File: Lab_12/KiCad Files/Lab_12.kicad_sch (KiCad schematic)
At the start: 35 parts

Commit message: Continue Lab 12
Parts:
- added C? (x2): 0.01uF, symbol Device:C
- added D?: 9.1V, symbol Device:D_Zener
- added LD?: D_Laser_1C2A, symbol Device:D_Laser_1C2A
- added Q?: Q_NPN_EBC, symbol Device:Q_NPN_EBC
- added R?: 100K, Resistor_THT:R_Axial_DIN0207_L6.3mm_D2.5mm_P7.62mm_Horizontal, symbol Device:R
- added R? (x2): 1K, Resistor_THT:R_Axial_DIN0207_L6.3mm_D2.5mm_P7.62mm_Horizontal, symbol Device:R
- added R?: 330K, Resistor_THT:R_Axial_DIN0207_L6.3mm_D2.5mm_P7.62mm_Horizontal, symbol Device:R
- added R?: 10K, Resistor_THT:R_Axial_DIN0207_L6.3mm_D2.5mm_P7.62mm_Horizontal, symbol Device:R
- added SC?: Solar_Cell, symbol Device:Solar_Cell
- added U? (x3): TLV272, symbol Amplifier_Operational:TLV2372
- D?: value 5.1V -> 6.2V
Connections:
- net GND: now also C?.2, Q?.1 (E), R?.2, R?.2, SC?.2 (-), U?.4 (V-)
- net V_Supply: now also D?.1 (K)
- net at U?.1: now also C?.1, R?.1
- net at U?.2: now also R?.1, R?.2
- net +5V renamed +6V
- net +6V: now also U?.8 (V+)
- new net: C?.1, SC?.1 (+)
- new net: Q?.2 (B), R?.2
- new net: LD?.1 (K), Q?.3 (C)
- new net: C?.2, R?.1, U?.3 (+)
- new net: D?.2 (A), LD?.2 (A)
- new net: R?.1, U?.1
- new net: R?.1, R?.2, U?.2 (-)
- no-connect marks 11 -> 13
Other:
- note added: "Laser Driver"
- moved on the sheet: C?, D?, M?, R?, RV?, U?, U?A, U?B, U?C, U?D, U?E, U?F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

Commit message: Continue Lab 12 Schema
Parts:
- removed R?: 680K, Resistor_THT:R_Axial_DIN0207_L6.3mm_D2.5mm_P7.62mm_Horizontal, symbol Device:R
- removed U? (x3): TLV272, symbol Amplifier_Operational:TLV2372
- added C? (x3): 0.22uF, symbol Device:C
- added C?: 0.1uF, symbol Device:C
- added D? (x2): 1N4148, symbol Device:D
- added R?: 680K, Resistor_THT:R_Axial_DIN0207_L6.3mm_D2.5mm_P7.62mm_Horizontal, symbol Device:R
- added R? (x6): 100K, Resistor_THT:R_Axial_DIN0207_L6.3mm_D2.5mm_P7.62mm_Horizontal, symbol Device:R
- added R? (x2): 6K8, Resistor_THT:R_Axial_DIN0207_L6.3mm_D2.5mm_P7.62mm_Horizontal, symbol Device:R
- added R?: 270K, Resistor_THT:R_Axial_DIN0207_L6.3mm_D2.5mm_P7.62mm_Horizontal, symbol Device:R
- added R?: 470K, Resistor_THT:R_Axial_DIN0207_L6.3mm_D2.5mm_P7.62mm_Horizontal, symbol Device:R
- added R? (x2): 4M7, Resistor_THT:R_Axial_DIN0207_L6.3mm_D2.5mm_P7.62mm_Horizontal, symbol Device:R
- added R? (x2): 4K7, Resistor_THT:R_Axial_DIN0207_L6.3mm_D2.5mm_P7.62mm_Horizontal, symbol Device:R
- added R? (x2): 2M2, Resistor_THT:R_Axial_DIN0207_L6.3mm_D2.5mm_P7.62mm_Horizontal, symbol Device:R
- added R?: 47K, Resistor_THT:R_Axial_DIN0207_L6.3mm_D2.5mm_P7.62mm_Horizontal, symbol Device:R
- added R?: 1K, Resistor_THT:R_Axial_DIN0207_L6.3mm_D2.5mm_P7.62mm_Horizontal, symbol Device:R
- added RV? (x2): 200K, symbol Device:R_Potentiometer_Trim
- added RV?: 100K, symbol Device:R_Potentiometer_Trim
- added RV? (x2): 500K, SamacSys_Parts:3386P1503, symbol Device:R_Potentiometer_Trim
- added RV?: 100K, symbol Device:R_Potentiometer
- added RV?: 100K, SamacSys_Parts:3386P1503, symbol Device:R_Potentiometer_Trim
- added SW?: CW, symbol Switch:SW_Push
- added SW?: CCW, symbol Switch:SW_Push
- added U? (x3): TLV272, symbol Amplifier_Operational:TLV2372
- R?: value 1K -> 10K
- R?: value 330K -> 3M3
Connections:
- net +6V: now also RV?.1, U?.9 (EN3,4), R?.1, R?.1, R?.1, RV?.1, SW?.2, U?.8 (V+); no longer U?.1 (EN1,2)
- net GND: now also RV?.3, C?.2, C?.2, R?.2, R?.2, RV?.2, RV?.3, RV?.3, SW?.1, U?.4 (V-)
- net at RV?.2: now also R?.1
- net at U?.10 (3A): now also U?.8
- net at U?.11 (3Y): now also C?.1, M?.1 (+)
- net at U?.14 (4Y): now also C?.2, M?.2 (-)
- net at U?.15 (4A): now also R?.2, R?.2, U?.1, U?.9
- net at U?.2 (1A): no longer U?.8
- net at C?.2, R?.1: now also U?.3 (+)
- net at R?.1, U?.14 (X): now also R?.1, R?.2
- net at R?.1: now also U?.10 (-), C?.1, D?.1 (K), R?.1, R?.1
- net at R?.1, R?.2: now also U?.2 (-)
- net at U?.11 (+): now also R?.1, RV?.2
- net at U?.13: now also U?.11 (A), D?.1 (K), R?.2, R?.2
- net at U?.12 (X0): now also U?.14, R?.2
- net at U?.13 (X1): now also U?.12
- net at U?.13: now also RV?.2
- net SGND: now reaches U?.5 (+)
- net SGND: now also U?.10 (+), U?.12 (+), U?.3 (+), C?.1, R?.1, R?.1, R?.2
- net at U?.6 (-): now also C?.1, RV?.1, RV?.2
- net at U?.7: now also C?.2, R?.1
- net at U?.13 (-): now also R?.1, R?.2, R?.2, R?.2
- new net: R?.2, RV?.1
- new net: R?.1, RV?.1, RV?.2, U?.1
- new net: R?.2, R?.2, U?.5 (+)
- new net: C?.1, R?.2
- new net: C?.2, RV?.3, U?.9 (-)
- new net: RV?.1, RV?.3
- new net: R?.2, SW?.2
- new net: D?.2 (A), U?.1
- new net: R?.1, RV?.1, RV?.2, U?.8
- new net: RV?.1, RV?.2, RV?.3
- new net: R?.1, R?.2, U?.6 (-)
- new net: R?.1, R?.1, R?.2, RV?.3, U?.7
- new net: R?.1, SW?.1
- new net: R?.2, RV?.3, U?.2 (-)
- now unconnected: U?.3 (1Y), U?.6 (2Y), U?.7 (2A)
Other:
- note added: "D"
- note added: "Error Amplifier"
- note added: "Feedback Mux & Jog Control"
- note added: "High Rotation Limit Trim"
- note added: "I"
- note added: "Laser Presence Detector"
- note added: "Laser Presence Threshold Trim"
- note added: "Low Rotation Limit Trim"
- note added: "P"
- note added: "P.I.D. Controller"
- note added: "Peak Detector"
- note added: "Setpoint Trim"
- note added: "Solar Cell Filter & Amplifier"
- note added: "~1kHz Pulse"
- note removed: "Voltage Feedback"
- moved on the sheet: C?, D?, LD?, M?, Q?, R?, RV?, SC?, U?, U?A, U?B, U?C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

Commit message: Finish Lab 12 Schema Rev1
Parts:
- removed D?: 1N4148, symbol Device:D
- removed R?: 6K8, Resistor_THT:R_Axial_DIN0207_L6.3mm_D2.5mm_P7.62mm_Horizontal, symbol Device:R
- removed RV? (x2): 200K, symbol Device:R_Potentiometer_Trim
- added R15, R16: 1M5, Resistor_THT:R_Axial_DIN0207_L6.3mm_D2.5mm_P7.62mm_Horizontal, symbol Device:R
- C1, C2, C4: renamed from C?; footprint (none) -> Capacitor_THT:C_Rect_L16.5mm_W4.7mm_P15.00mm_MKT
- C3, C5, C6, C8, C9: renamed from C?; footprint (none) -> Capacitor_THT:C_Disc_D9.0mm_W2.5mm_P5.00mm
- C7: renamed from C?; footprint (none) -> Capacitor_THT:C_Disc_D9.0mm_W5.0mm_P10.00mm
- D1, D2: renamed from D?; footprint (none) -> Diode_THT:D_A-405_P7.62mm_Horizontal
- D3: renamed from D?; footprint (none) -> Diode_THT:D_A-405_P12.70mm_Horizontal
- LD1: renamed from LD?; footprint (none) -> Connector_PinHeader_2.54mm:PinHeader_1x02_P2.54mm_Vertical
- M1: renamed from M?; footprint (none) -> Connector_PinHeader_2.54mm:PinHeader_1x02_P2.54mm_Vertical
- Q1: renamed from Q?; value Q_NPN_EBC -> 2N4401; footprint (none) -> Package_TO_SOT_THT:TO-92L_Inline_Wide
- R29: renamed from R?; footprint Resistor_THT:R_Axial_DIN0207_L6.3mm_D2.5mm_P7.62mm_Horizontal -> Resistor_THT:R_Axial_DIN0207_L6.3mm_D2.5mm_P2.54mm_Vertical
- R3: renamed from R?; footprint Resistor_THT:R_Axial_DIN0207_L6.3mm_D2.5mm_P7.62mm_Horizontal -> Resistor_THT:R_Axial_DIN0207_L6.3mm_D2.5mm_P10.16mm_Horizontal
- RV1: renamed from RV?; value 100K -> 2M; footprint (none) -> Connector_PinHeader_2.54mm:PinHeader_1x03_P2.54mm_Vertical
- RV6: renamed from RV?; footprint (none) -> SamacSys_Parts:3386P1503
- SC1: renamed from SC?; footprint (none) -> Connector_PinHeader_2.54mm:PinHeader_1x02_P2.54mm_Vertical
- SW1, SW2: renamed from SW?; footprint (none) -> Button_Switch_THT:SW_PUSH_6mm_H9.5mm
- U1: renamed from U?; footprint (none) -> Package_DIP:DIP-8_W7.62mm
- U2, U3, U4: renamed from U?; footprint (none) -> Package_DIP:DIP-14_W7.62mm
- U5: renamed from U?; footprint (none) -> Package_DIP:DIP-16_W7.62mm
- gave numbers to parts that had none: 35
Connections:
- net +6V: now also R15.1
- net GND: now also R16.2
- net at RV1.3: now also R16.1
- net at RV1.1: now also R15.2
- no-connect marks 13 -> 22
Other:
- note added: "Scanning Circuitry"
- note removed: "High Rotation Limit Trim"
- note removed: "Low Rotation Limit Trim"
- moved on the sheet: RV1, U3B, U3C, U3E, U3F, U4D

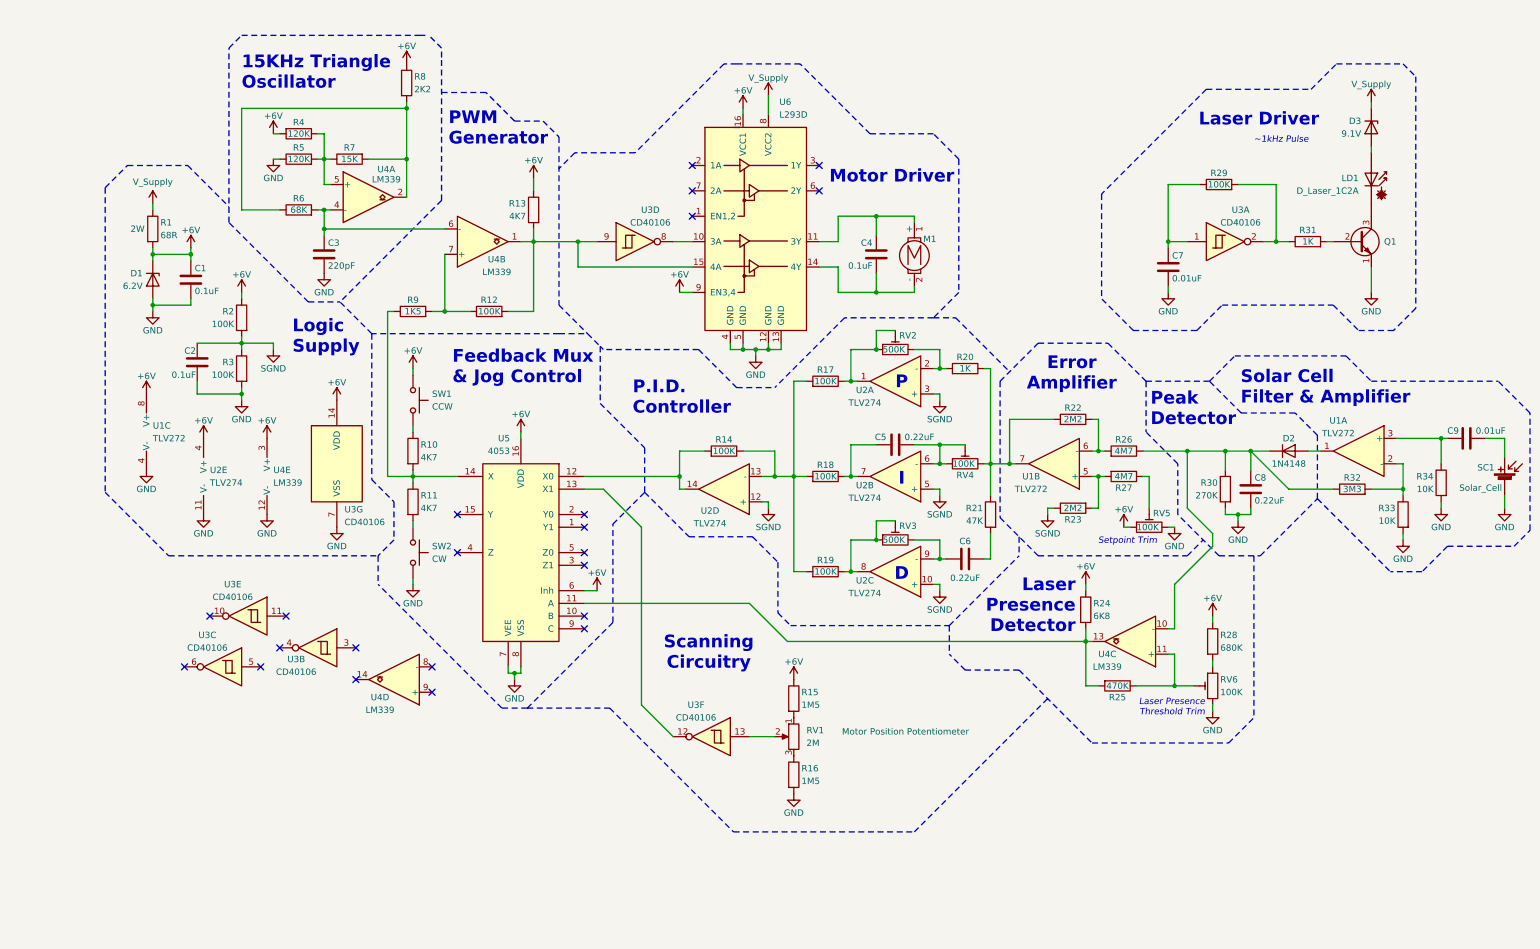
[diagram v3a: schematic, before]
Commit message: Connect Unused 40106 Inputs to GND
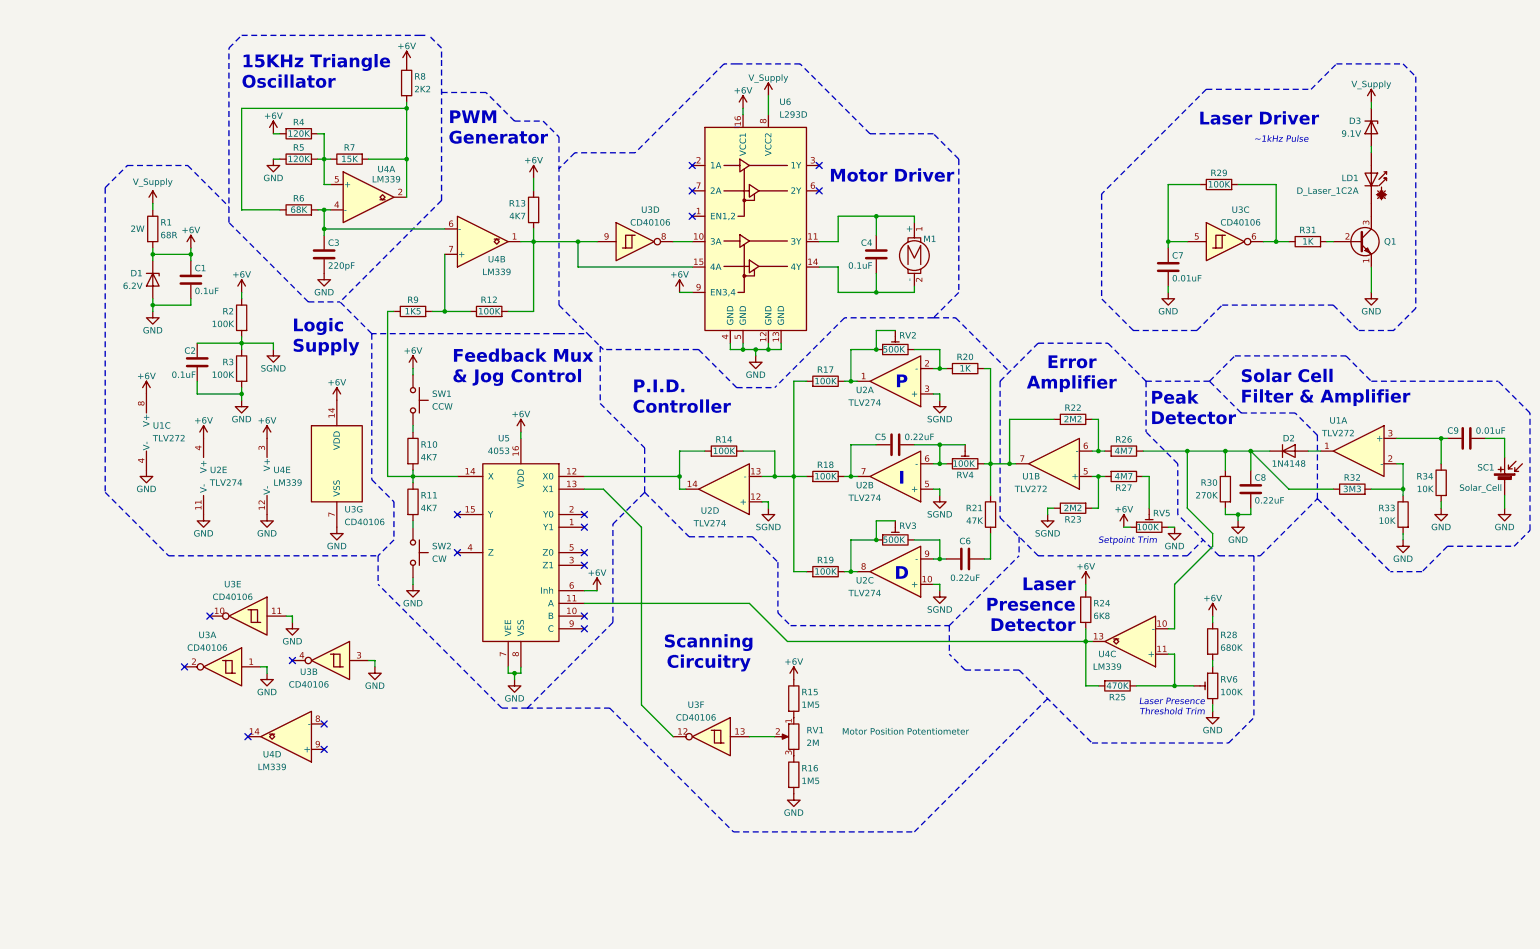
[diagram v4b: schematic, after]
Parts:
- C8: footprint Capacitor_THT:C_Disc_D9.0mm_W2.5mm_P5.00mm -> Capacitor_THT:C_Disc_D9.0mm_W5.0mm_P7.50mm
- D2: footprint Diode_THT:D_A-405_P7.62mm_Horizontal -> Diode_THT:D_A-405_P2.54mm_Vertical_AnodeUp
- R12, R25, R31, R32, R6: footprint Resistor_THT:R_Axial_DIN0207_L6.3mm_D2.5mm_P7.62mm_Horizontal -> Resistor_THT:R_Axial_DIN0207_L6.3mm_D2.5mm_P5.08mm_Vertical
- R13, R24, R28, R33, R34, R5: footprint Resistor_THT:R_Axial_DIN0207_L6.3mm_D2.5mm_P7.62mm_Horizontal -> Resistor_THT:R_Axial_DIN0207_L6.3mm_D2.5mm_P10.16mm_Horizontal
- R14, R17, R18, R21, R22: footprint Resistor_THT:R_Axial_DIN0207_L6.3mm_D2.5mm_P7.62mm_Horizontal -> Resistor_THT:R_Axial_DIN0207_L6.3mm_D2.5mm_P2.54mm_Vertical
- R19, R23: footprint Resistor_THT:R_Axial_DIN0207_L6.3mm_D2.5mm_P7.62mm_Horizontal -> Resistor_THT:R_Axial_DIN0207_L6.3mm_D2.5mm_P15.24mm_Horizontal
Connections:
- net GND: now also U3.1, U3.11, U3.3
- net at C7.1, R29.1: now also U3.5; no longer U3.1
- net at R29.2, R31.1: now also U3.6; no longer U3.2
- no-connect marks 22 -> 19
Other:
- moved on the sheet: U3B, U4D

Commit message: Finish Lab 12
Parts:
- removed R15: 1M5, Resistor_THT:R_Axial_DIN0207_L6.3mm_D2.5mm_P7.62mm_Horizontal, symbol Device:R
- added R14: 2K2, Resistor_THT:R_Axial_DIN0207_L6.3mm_D2.5mm_P10.16mm_Horizontal, symbol Device:R
- added R20, R21: 120K, Resistor_THT:R_Axial_DIN0207_L6.3mm_D2.5mm_P10.16mm_Horizontal, symbol Device:R
- C3: value 220pF -> 100pF
- R16: value 1M5 -> 15K; footprint Resistor_THT:R_Axial_DIN0207_L6.3mm_D2.5mm_P7.62mm_Horizontal -> Resistor_THT:R_Axial_DIN0207_L6.3mm_D2.5mm_P5.08mm_Vertical
- R27: renamed from R25; footprint Resistor_THT:R_Axial_DIN0207_L6.3mm_D2.5mm_P5.08mm_Vertical -> Resistor_THT:R_Axial_DIN0207_L6.3mm_D2.5mm_P15.24mm_Horizontal
- renumbered R14 to R15, R20 to R22, R21 to R23, R22 to R24, R23 to R25, R24 to R26, R26 to R28, R27 to R29, R28 to R30, R29 to R31, R30 to R32, R31 to R33, R32 to R34, R33 to R35, R34 to R36
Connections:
- net +6V: now also RV1.1, R14.1, R20.1
- net GND: now also RV1.3, RV6.1, U3.13, R21.2; no longer R16.2, RV6.3
- net at R30.2: now also RV6.3; no longer RV6.1
- net at R26.2, R27.2, U5.11 (A): now also U4.14; no longer U4.13
- net at C8.1, D2.1 (K), R28.1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: now also U4.8 (-); no longer U4.10 (-)
- net at R27.1, RV6.2: now also U4.9 (+); no longer U4.11 (+)
- net at R16.1: now also U4.11 (+), R20.2, R21.1; no longer RV1.3
- net at RV1.2: now also U4.10 (-); no longer U3.13
- net at U5.13 (X1): now also R16.2, U4.13, R14.2; no longer U3.12
- no-connect marks 19 -> 17
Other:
- note added: "30KHz Triangle Oscillator"
- note removed: "15KHz Triangle Oscillator"
- moved on the sheet: RV1, RV6, U3A, U3B, U3E, U3F, U4C
